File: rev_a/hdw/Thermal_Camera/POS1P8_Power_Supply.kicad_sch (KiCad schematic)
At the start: 23 parts

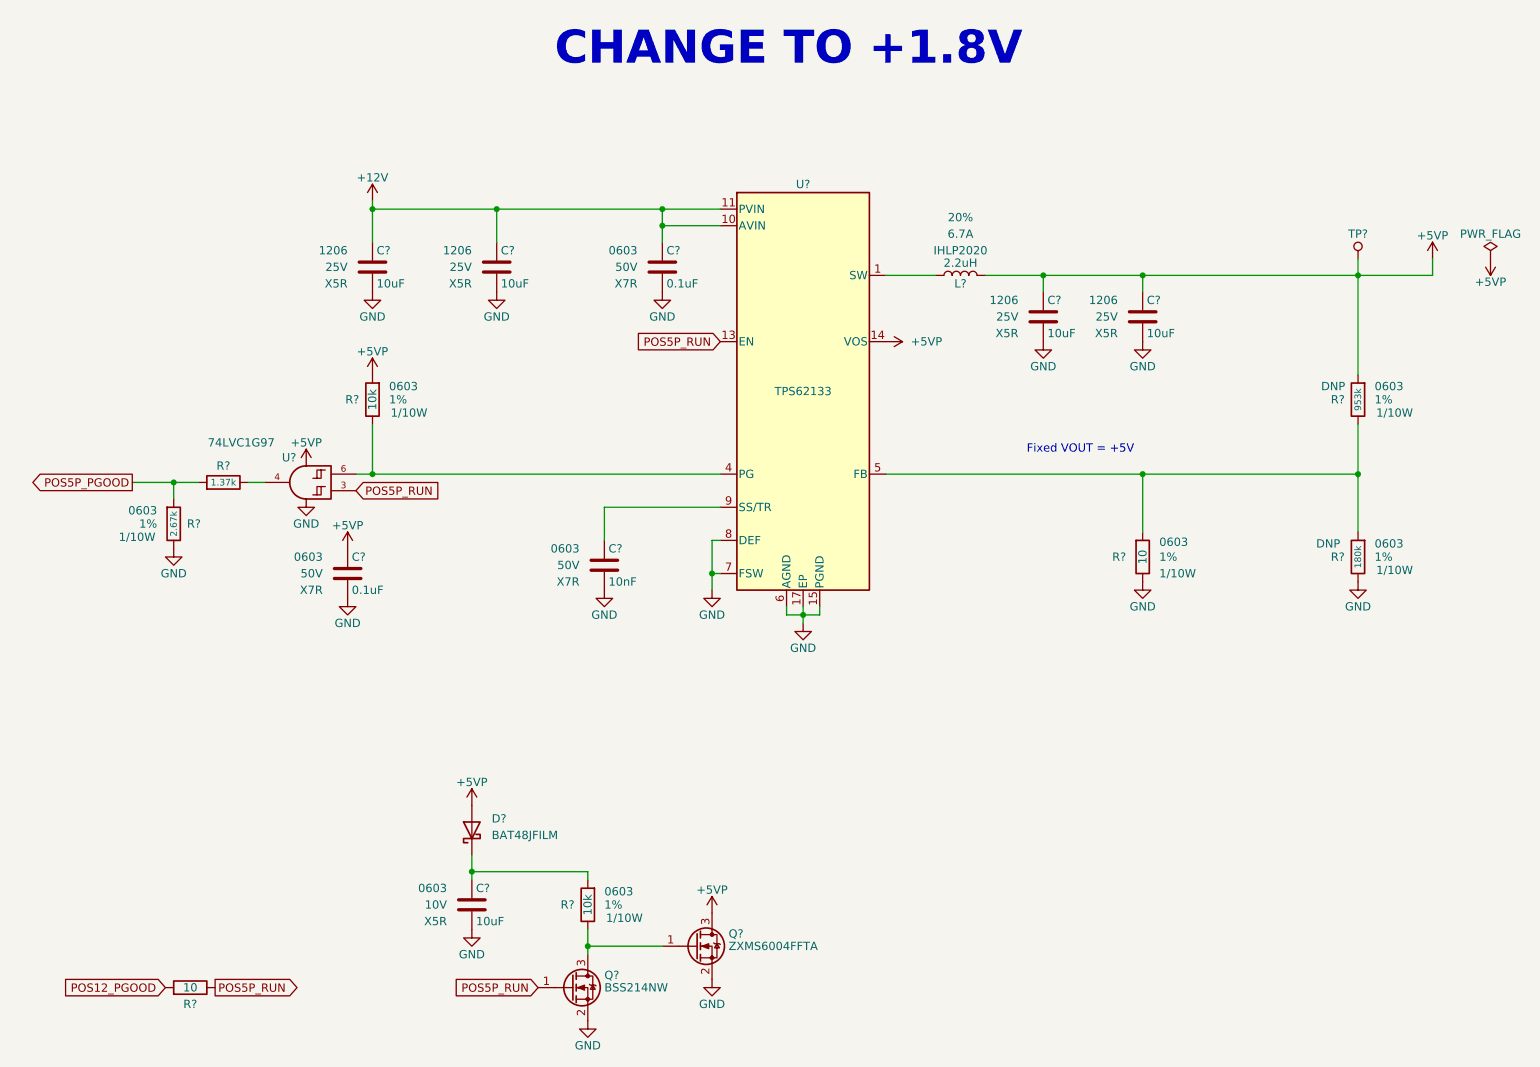
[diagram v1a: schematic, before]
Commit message: added many more blank schematic sheets
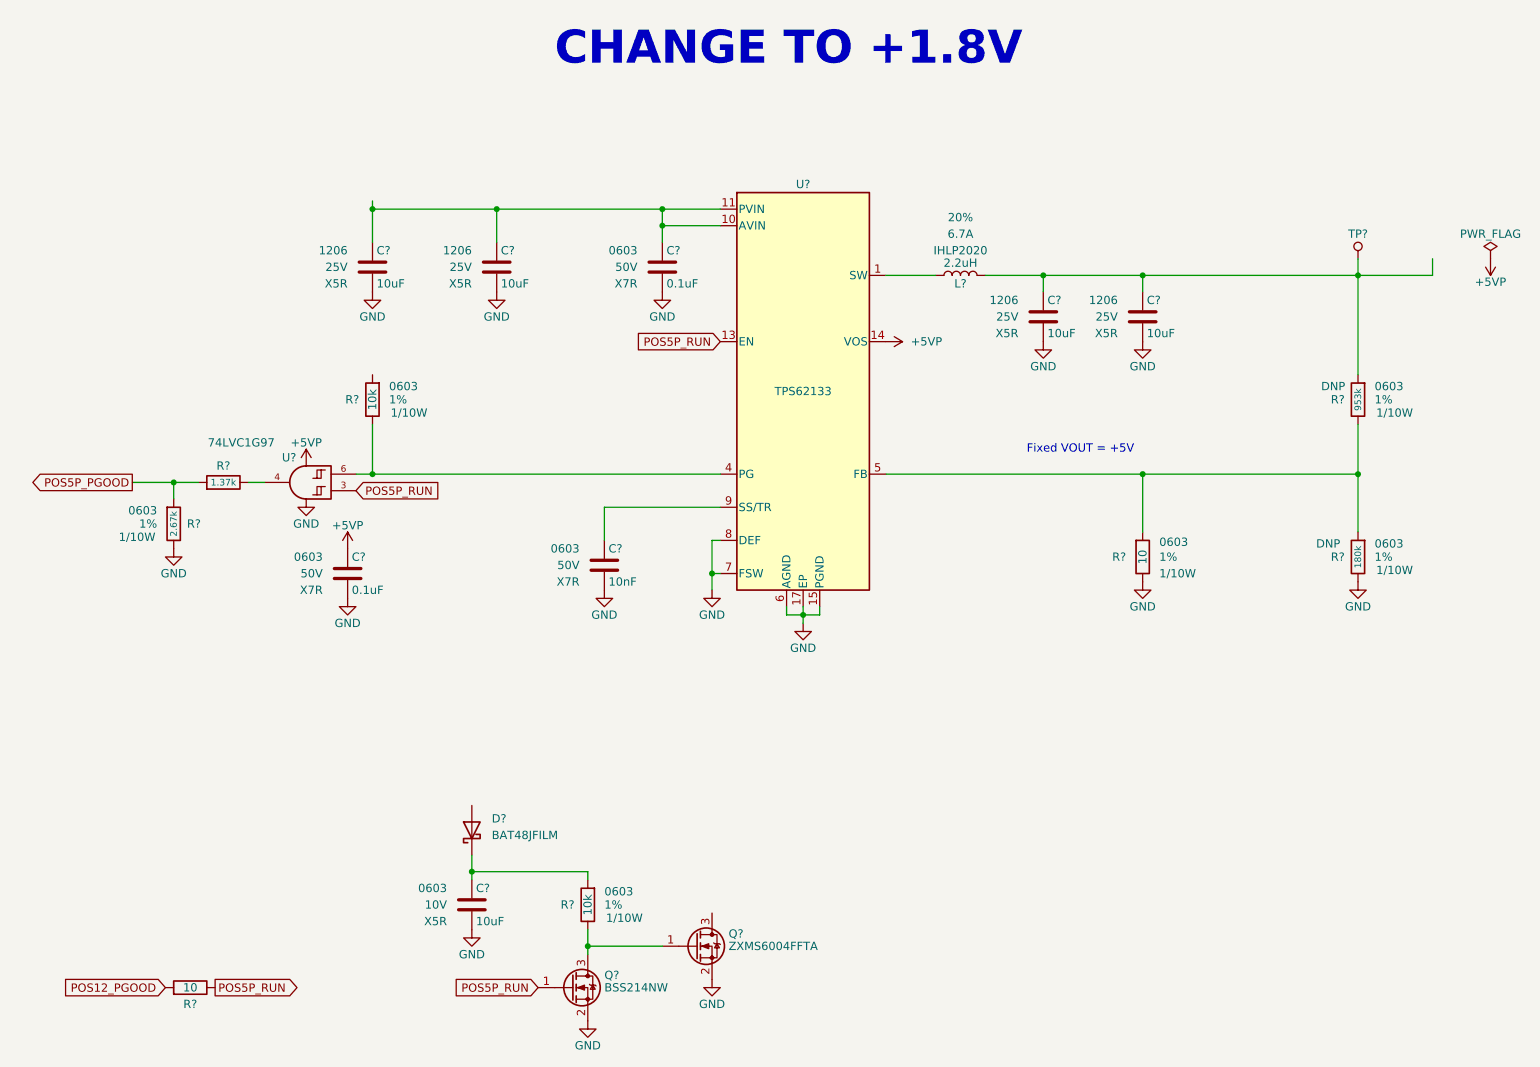
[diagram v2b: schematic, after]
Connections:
- net +5VP: no longer C?.1, C?.1, D?.2 (A), L?.2, Q?.3 (D), R?.1, R?.1, TP?.1 (TP)
- net +12V: no longer names the net of C?.1, C?.1, C?.1, U?.10 (AVIN), U?.11 (PVIN), U?.12 (PVIN)
- new net: C?.1, C?.1, L?.2, R?.1, TP?.1 (TP)
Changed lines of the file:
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@@
   (title_block
     (title "Thermal Camera")
-    (date "2023-11-12")
+    (date "2023-11-13")
     (rev "PRELIM")
     (company "Drew Maatman and Michael Laffin")
@@
         (path "/e85aac8c-404c-45dd-bda3-1057cae83baf/00000000-0000-0000-0000-00005f41a7c7"
           (reference "C307") (unit 1)
-        )
-      )
-    )
-  )
-  (symbol (lib_id "power:+5VP") (at 125.73 157.48 0) (unit 1)
-    (in_bom yes) (on_board yes) (dnp no)
-    (property "Reference" "#PWR0416" (at 125.73 161.29 0)
-      (effects (font (size 1.27 1.27)) hide)
-    )
-    (property "Value" "+5VP" (at 125.73 153.924 0)
-      (effects (font (size 1.27 1.27)))
-    )
-    (property "Footprint" "" (at 125.73 157.48 0)
-      (effects (font (size 1.27 1.27)) hide)
-    )
-    (property "Datasheet" "" (at 125.73 157.48 0)
-      (effects (font (size 1.27 1.27)) hide)
-    )
-    (pin "1")
-    (instances
-      (project "Thermal_Camera"
-        (path "/4bd21e0b-5408-4b93-866e-c82ac5b31fa9/3996b81d-92d5-40b5-9537-6a34278c1c5b"
-          (reference "#PWR0416") (unit 1)
-        )
-        (path "/4bd21e0b-5408-4b93-866e-c82ac5b31fa9/3fa2ed45-8dc3-4842-ae64-2bab78bff715"
-          (reference "#PWR0616") (unit 1)
-        )
-      )
-      (project "USB_Hub"
-        (path "/e85aac8c-404c-45dd-bda3-1057cae83baf/00000000-0000-0000-0000-00005f41a7c7"
-          (reference "#PWR0315") (unit 1)
-        )
-      )
-    )
-  )
-  (symbol (lib_id "power:+5VP") (at 73.66 74.93 0) (unit 1)
-    (in_bom yes) (on_board yes) (dnp no)
-    (property "Reference" "#PWR0408" (at 73.66 78.74 0)
-      (effects (font (size 1.27 1.27)) hide)
-    )
-    (property "Value" "+5VP" (at 73.66 71.374 0)
-      (effects (font (size 1.27 1.27)))
-    )
-    (property "Footprint" "" (at 73.66 74.93 0)
-      (effects (font (size 1.27 1.27)) hide)
-    )
-    (property "Datasheet" "" (at 73.66 74.93 0)
-      (effects (font (size 1.27 1.27)) hide)
-    )
-    (pin "1")
-    (instances
-      (project "Thermal_Camera"
-        (path "/4bd21e0b-5408-4b93-866e-c82ac5b31fa9/3996b81d-92d5-40b5-9537-6a34278c1c5b"
-          (reference "#PWR0408") (unit 1)
-        )
-        (path "/4bd21e0b-5408-4b93-866e-c82ac5b31fa9/3fa2ed45-8dc3-4842-ae64-2bab78bff715"
-          (reference "#PWR0608") (unit 1)
-        )
-      )
-      (project "USB_Hub"
-        (path "/e85aac8c-404c-45dd-bda3-1057cae83baf/00000000-0000-0000-0000-00005f41a7c7"
-          (reference "#PWR0308") (unit 1)
         )
       )
@@
     )
   )
-  (symbol (lib_id "power:+12V") (at 73.66 48.26 0) (unit 1)
-    (in_bom yes) (on_board yes) (dnp no)
-    (property "Reference" "#PWR0406" (at 73.66 52.07 0)
-      (effects (font (size 1.27 1.27)) hide)
-    )
-    (property "Value" "+12V" (at 73.66 44.704 0)
-      (effects (font (size 1.27 1.27)))
-    )
-    (property "Footprint" "" (at 73.66 48.26 0)
-      (effects (font (size 1.27 1.27)) hide)
-    )
-    (property "Datasheet" "" (at 73.66 48.26 0)
-      (effects (font (size 1.27 1.27)) hide)
-    )
-    (pin "1")
-    (instances
-      (project "Thermal_Camera"
-        (path "/4bd21e0b-5408-4b93-866e-c82ac5b31fa9/3996b81d-92d5-40b5-9537-6a34278c1c5b"
-          (reference "#PWR0406") (unit 1)
-        )
-        (path "/4bd21e0b-5408-4b93-866e-c82ac5b31fa9/3fa2ed45-8dc3-4842-ae64-2bab78bff715"
-          (reference "#PWR0606") (unit 1)
-        )
-      )
-      (project "LED_Panel_Controller"
-        (path "/9a153a92-537f-48f9-b716-589877e287a5/00000000-0000-0000-0000-00005e0dc082"
-          (reference "#PWR?") (unit 1)
-        )
-        (path "/9a153a92-537f-48f9-b716-589877e287a5/00000000-0000-0000-0000-00005eae2d8a"
-          (reference "#PWR?") (unit 1)
-        )
-        (path "/9a153a92-537f-48f9-b716-589877e287a5/00000000-0000-0000-0000-00005cb7718d"
-          (reference "#PWR?") (unit 1)
-        )
-        (path "/9a153a92-537f-48f9-b716-589877e287a5/00000000-0000-0000-0000-00005f581ba3"
-          (reference "#PWR?") (unit 1)
-        )
-        (path "/9a153a92-537f-48f9-b716-589877e287a5/00000000-0000-0000-0000-00005e0f263a"
-          (reference "#PWR?") (unit 1)
-        )
-      )
-      (project "USB_Hub"
-        (path "/e85aac8c-404c-45dd-bda3-1057cae83baf/00000000-0000-0000-0000-00005f41a7c7"
-          (reference "#PWR0306") (unit 1)
-        )
-      )
-    )
-  )
   (symbol (lib_id "power:+5VP") (at 63.5 88.9 0) (unit 1)
     (in_bom yes) (on_board yes) (dnp no)
@@
         (path "/e85aac8c-404c-45dd-bda3-1057cae83baf/00000000-0000-0000-0000-00005f41a7c7"
           (reference "#PWR0305") (unit 1)
-        )
-      )
-    )
-  )
-  (symbol (lib_id "power:+5VP") (at 88.9 140.97 0) (unit 1)
-    (in_bom yes) (on_board yes) (dnp no)
-    (property "Reference" "#PWR0409" (at 88.9 144.78 0)
-      (effects (font (size 1.27 1.27)) hide)
-    )
-    (property "Value" "+5VP" (at 88.9 137.414 0)
-      (effects (font (size 1.27 1.27)))
-    )
-    (property "Footprint" "" (at 88.9 140.97 0)
-      (effects (font (size 1.27 1.27)) hide)
-    )
-    (property "Datasheet" "" (at 88.9 140.97 0)
-      (effects (font (size 1.27 1.27)) hide)
-    )
-    (pin "1")
-    (instances
-      (project "Thermal_Camera"
-        (path "/4bd21e0b-5408-4b93-866e-c82ac5b31fa9/3996b81d-92d5-40b5-9537-6a34278c1c5b"
-          (reference "#PWR0409") (unit 1)
-        )
-        (path "/4bd21e0b-5408-4b93-866e-c82ac5b31fa9/3fa2ed45-8dc3-4842-ae64-2bab78bff715"
-          (reference "#PWR0609") (unit 1)
-        )
-      )
-      (project "USB_Hub"
-        (path "/e85aac8c-404c-45dd-bda3-1057cae83baf/00000000-0000-0000-0000-00005f41a7c7"
-          (reference "#PWR0309") (unit 1)
         )
       )
@@
         )
       )
-    )
-  )
-  (symbol (lib_id "power:+5VP") (at 236.22 57.15 0) (unit 1)
-    (in_bom yes) (on_board yes) (dnp no)
-    (property "Reference" "#PWR0424" (at 236.22 60.96 0)
-      (effects (font (size 1.27 1.27)) hide)
-    )
-    (property "Value" "+5VP" (at 236.22 53.594 0)
-      (effects (font (size 1.27 1.27)))
-    )
-    (property "Footprint" "" (at 236.22 57.15 0)
-      (effects (font (size 1.27 1.27)) hide)
-    )
-    (property "Datasheet" "" (at 236.22 57.15 0)
-      (effects (font (size 1.27 1.27)) hide)
-    )
-    (pin "1")
-    (instances
-      (project "Thermal_Camera"
-        (path "/4bd21e0b-5408-4b93-866e-c82ac5b31fa9/3996b81d-92d5-40b5-9537-6a34278c1c5b"
-          (reference "#PWR0424") (unit 1)
-        )
-        (path "/4bd21e0b-5408-4b93-866e-c82ac5b31fa9/3fa2ed45-8dc3-4842-ae64-2bab78bff715"
-          (reference "#PWR0624") (unit 1)
-        )
-      )
-      (project "USB_Hub"
-        (path "/e85aac8c-404c-45dd-bda3-1057cae83baf/00000000-0000-0000-0000-00005f41a7c7"
-          (reference "#PWR0323") (unit 1)
-        )
-      )

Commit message: added some power supplies
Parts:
- removed R?: 10, Resistors_SMD:R_0603, symbol Custom_Library:R_Custom
- removed R?: 1.37k, Resistors_SMD:R_0603, symbol Custom_Library:R_Custom
- removed R?: 2.67k, Resistors_SMD:R_0603, symbol Custom_Library:R_Custom
- added R?: 10k, Resistors_SMD:R_0603, symbol Custom_Library:R_Custom
- R?: value 180k -> 1.5k; Configuration DNP -> (none); Digi-Key PN 541-180KHCT-ND -> (none)
- R?: value 953k -> 1.87k; Configuration DNP -> (none); Digi-Key PN 541-953KHCT-ND -> (none)
- U?: value TPS62133 -> TPS62130A; Digi-Key PN 296-30225-1-ND -> 296-39446-1-ND
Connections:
- net GND: now also R?.2
- net +1.8V: now reaches C?.1, C?.1, L?.2, R?.1, TP?.1 (TP)
- net +1.8V: now also Q?.3 (D), U?.14 (VOS)
- net VBAT: now reaches C?.1, C?.1, C?.1, U?.10 (AVIN), U?.11 (PVIN), U?.12 (PVIN)
- net POS1P8_PGOOD: now reaches U?.4
- net POS1P8_PGOOD: now also R?.1
- net +3.3V: now reaches R?.1
- net +3.3V: now also C?.1, D?.2 (A), U?.5 (VCC)
- removed net +5VP: C?.1, U?.14 (VOS), U?.5 (VCC)
- net POS5P_RUN renamed POS1P8_RUN
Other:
- note added: "figure out sequencing"
- note removed: "CHANGE TO +1.8V"
- note removed: "Fixed VOUT = +5V"
